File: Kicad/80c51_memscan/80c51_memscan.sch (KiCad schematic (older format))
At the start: 16 parts, among them J1 Conn_01x14_Male, J2 Conn_01x02_Male, SW1 SW_DPST_x2, U1 P80C51FA-4N,112, Y1 4-12Mhz

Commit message: Fixing typo 8051c -> 80c51.
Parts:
- U1: symbol 8051c_memscan-rescue:P80C51FA-4N,112-P80C51FA-4N_112 -> 80c51_memscan-rescue:P80C51FA-4N,112-P80C51FA-4N_112-8051c_memscan-rescue
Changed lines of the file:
@@
 EESchema Schematic File Version 4
-LIBS:8051c_memscan-cache
-EELAYER 29 0
+LIBS:80c51_memscan-cache
+EELAYER 26 0
 EELAYER END
 $Descr A4 11693 8268
 encoding utf-8
 Sheet 1 1
-Title "8051C Memory Scanner"
+Title "80C51 Memory Scanner"
 Date "2019-08-30"
 Rev "v1.0"
@@
 	3500 1900 3650 1900
 $Comp
-L 8051c_memscan-rescue:P80C51FA-4N,112-P80C51FA-4N_112 U1
+L 80c51_memscan-rescue:P80C51FA-4N,112-P80C51FA-4N_112-8051c_memscan-rescue U1
 U 1 1 5D70DC40
 P 5050 3550

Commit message: Folding in feedback. Adding led and additional pins to header.
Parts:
- added D1: LED, symbol Device:LED
- added R10: R, symbol Device:R
- J1: symbol Connector:Conn_01x14_Male -> Connector_Generic:Conn_02x16_Counter_Clockwise
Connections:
- net +5V: now also J1.17 (Pin_17), J1.18 (Pin_18), J1.19 (Pin_19), J1.20 (Pin_20), J1.21 (Pin_21), J1.22 (Pin_22), J1.23 (Pin_23), J1.24 (Pin_24), J1.25 (Pin_25), J1.26 (Pin_26), J1.27 (Pin_27), J1.28 (Pin_28), J1.29 (Pin_29), J1.30 (Pin_30), J1.31 (Pin_31), J1.32 (Pin_32), D1.2 (A), R10.2
- net 1 renamed A0
- net 10 renamed A9
- net 11 renamed A10
- net 12 renamed A11
- net 13 renamed A12
- net 14 renamed A13
- net 2 renamed A1
- net 3 renamed A2
- net 4 renamed A3
- net 5 renamed A4
- net 6 renamed A5
- net 7 renamed A6
- net 8 renamed A7
- net 9 renamed A8
- net xtal1 renamed XTAL1
- net xtal2 renamed XTAL2
- new net: D1.1 (K), R10.1
- no-connect marks 20 -> 22
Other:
- moved on the sheet: C1, C2, J2, R1, SW1A, U1, Y1

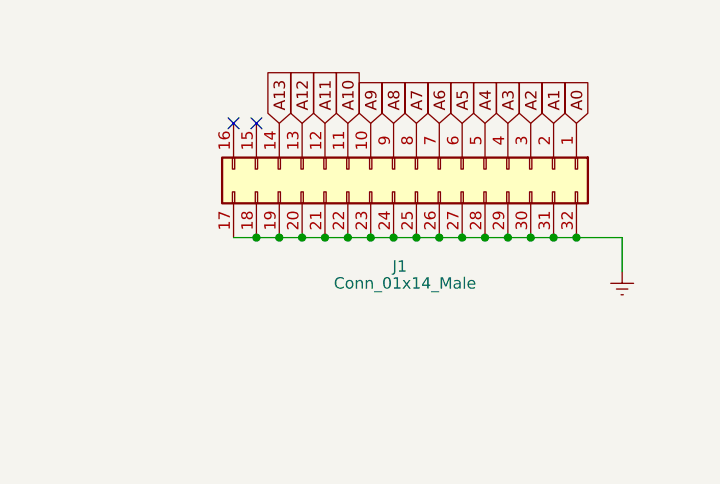
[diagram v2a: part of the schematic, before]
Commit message: Fix J1 text.
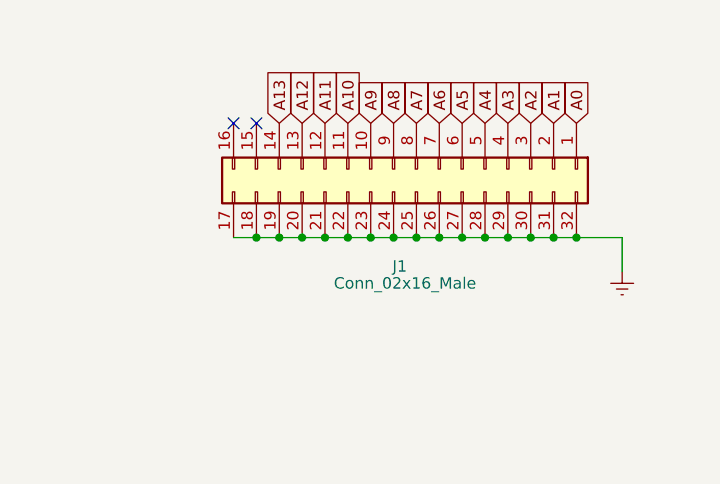
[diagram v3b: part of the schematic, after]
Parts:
- J1: value Conn_01x14_Male -> Conn_02x16_Male
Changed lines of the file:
@@
 P 8700 5000
 F 0 "J1" V 9126 4927 50  0000 C CNN
-F 1 "Conn_01x14_Male" V 9200 4950 50  0000 C CNN
+F 1 "Conn_02x16_Male" V 9200 4950 50  0000 C CNN
 F 2 "" H 8700 5000 50  0001 C CNN
 F 3 "~" H 8700 5000 50  0001 C CNN

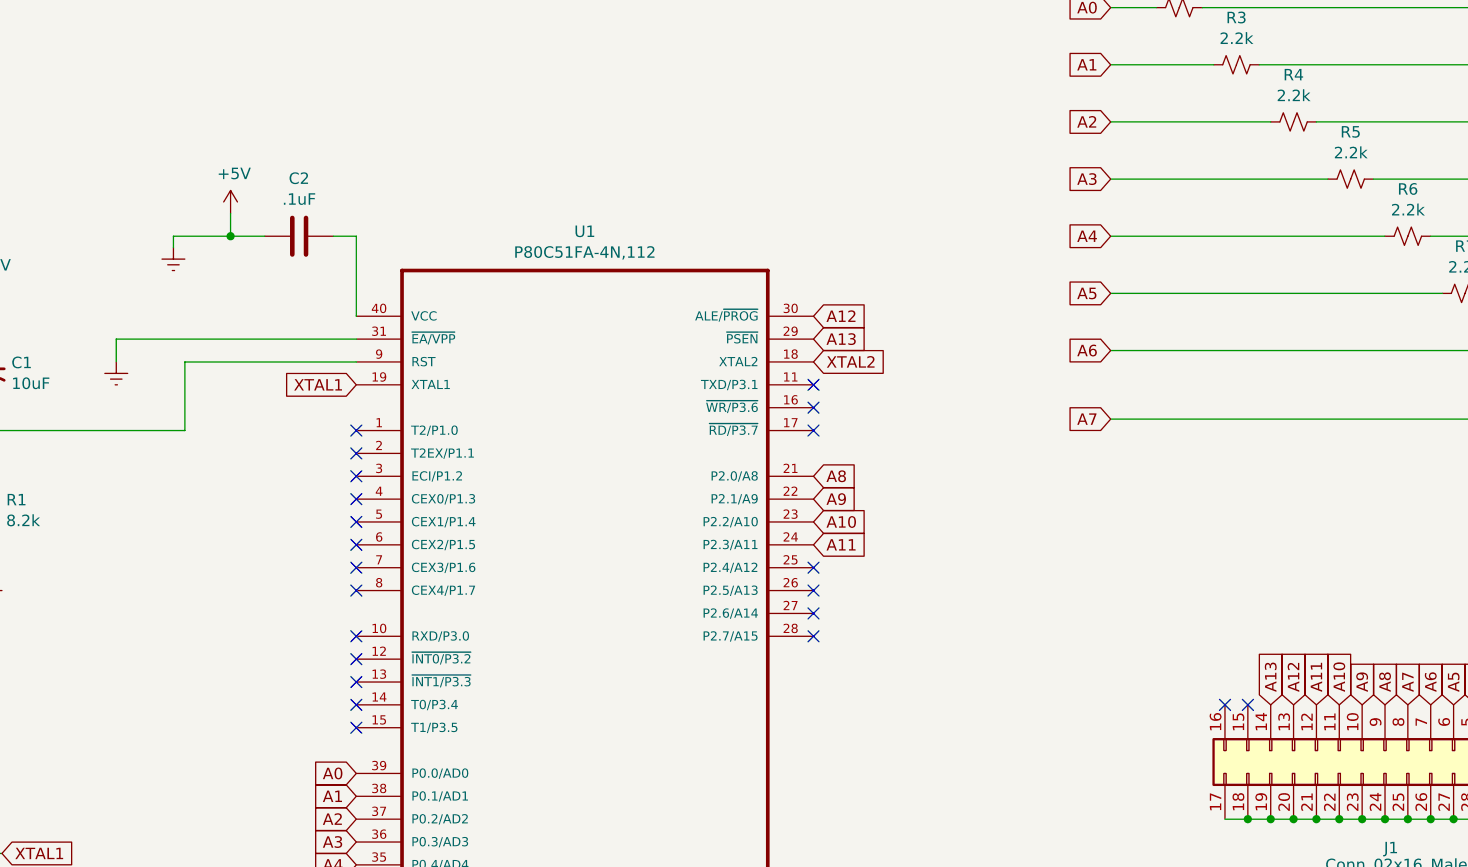
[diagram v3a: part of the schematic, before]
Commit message: Fixing bad cap wiring and some net names.
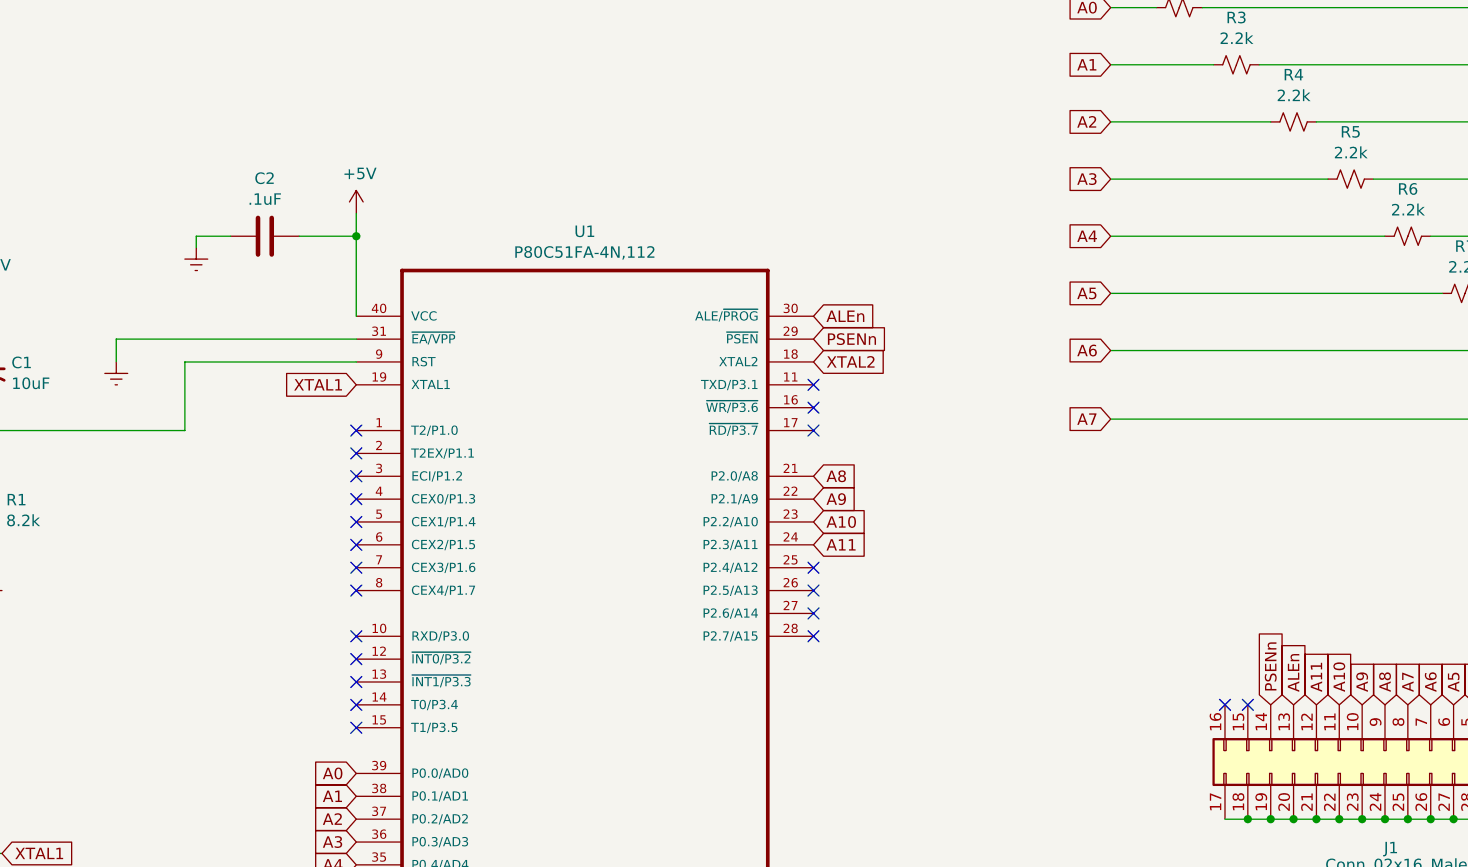
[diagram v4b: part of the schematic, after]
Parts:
- C1, C2, R1, R10, R2, R3, R4, R5, R6, R7, R8, R9: footprint (none) -> Capacitor_SMD:C_0603_1608Metric_Pad1.05x0.95mm_HandSolder
- D1: footprint (none) -> LED_SMD:LED_0603_1608Metric
- J1: footprint (none) -> Connector_PinHeader_2.54mm:PinHeader_2x16_P2.54mm_Vertical
- J2: footprint (none) -> Connector_PinHeader_2.54mm:PinHeader_1x02_P2.54mm_Vertical
- SW1: footprint (none) -> Button_Switch_SMD:SW_DIP_SPSTx02_Slide_6.7x6.64mm_W8.61mm_P2.54mm_LowProfile
- Y1: footprint (none) -> Crystal:Crystal_SMD_0603-2Pin_6.0x3.5mm_HandSoldering
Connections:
- net +5V: now also C2.2, U1.40 (VCC); no longer C2.1, J1.17 (Pin_17), J1.18 (Pin_18), J1.19 (Pin_19), J1.20 (Pin_20), J1.21 (Pin_21), J1.22 (Pin_22), J1.23 (Pin_23), J1.24 (Pin_24), J1.25 (Pin_25), J1.26 (Pin_26), J1.27 (Pin_27), J1.28 (Pin_28), J1.29 (Pin_29), J1.30 (Pin_30), J1.31 (Pin_31), J1.32 (Pin_32), J2.2 (Pin_2), R1.2, R10.2, R2.1, R3.1, R4.1, R5.1, R6.1, R7.1, R8.1, R9.1, U1.20 (VSS), U1.31 (~EA/VPP)
- net A12 renamed ALEn
- net A13 renamed PSENn
- new net Earth: C2.1, J1.17 (Pin_17), J1.18 (Pin_18), J1.19 (Pin_19), J1.20 (Pin_20), J1.21 (Pin_21), J1.22 (Pin_22), J1.23 (Pin_23), J1.24 (Pin_24), J1.25 (Pin_25), J1.26 (Pin_26), J1.27 (Pin_27), J1.28 (Pin_28), J1.29 (Pin_29), J1.30 (Pin_30), J1.31 (Pin_31), J1.32 (Pin_32), J2.2 (Pin_2), R1.2, R10.2, R2.1, R3.1, R4.1, R5.1, R6.1, R7.1, R8.1, R9.1, U1.20 (VSS), U1.31 (~EA/VPP)
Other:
- moved on the sheet: C2
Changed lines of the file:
@@
 F 0 "Y1" V 1904 5731 50  0000 L CNN
 F 1 "4-12Mhz" V 1995 5731 50  0000 L CNN
-F 2 "" H 1950 5600 50  0001 C CNN
+F 2 "Crystal:Crystal_SMD_0603-2Pin_6.0x3.5mm_HandSoldering" H 1950 5600 50  0001 C CNN
 F 3 "~" H 1950 5600 50  0001 C CNN
 	1    1950 5600
@@
 F 0 "C1" H 2591 3396 50  0000 L CNN
 F 1 "10uF" H 2591 3305 50  0000 L CNN
-F 2 "" H 2500 3350 50  0001 C CNN
+F 2 "Capacitor_SMD:C_0603_1608Metric_Pad1.05x0.95mm_HandSolder" H 2500 3350 50  0001 C CNN
 F 3 "~" H 2500 3350 50  0001 C CNN
 	1    2500 3350
@@
 F 0 "R1" H 2568 3996 50  0000 L CNN
 F 1 "8.2k" H 2568 3905 50  0000 L CNN
-F 2 "" H 2500 3950 50  0001 C CNN
+F 2 "Capacitor_SMD:C_0603_1608Metric_Pad1.05x0.95mm_HandSolder" H 2500 3950 50  0001 C CNN
 F 3 "~" H 2500 3950 50  0001 C CNN
 	1    2500 3950
@@
 L power:+5V #PWR05
 U 1 1 5D6AD917
-P 3550 2650
-F 0 "#PWR05" H 3550 2500 50  0001 C CNN
-F 1 "+5V" H 3565 2823 50  0000 C CNN
-F 2 "" H 3550 2650 50  0001 C CNN
-F 3 "" H 3550 2650 50  0001 C CNN
-	1    3550 2650
+P 4100 2650
+F 0 "#PWR05" H 4100 2500 50  0001 C CNN
+F 1 "+5V" H 4115 2823 50  0000 C CNN
+F 2 "" H 4100 2650 50  0001 C CNN
+F 3 "" H 4100 2650 50  0001 C CNN
+	1    4100 2650
 	1    0    0    -1
 $EndComp
@@
 F 0 "SW1" V 1746 3162 50  0000 R CNN
 F 1 "SW_DPST_x2" V 1655 3162 50  0000 R CNN
-F 2 "" H 1700 3250 50  0001 C CNN
+F 2 "Button_Switch_SMD:SW_DIP_SPSTx02_Slide_6.7x6.64mm_W8.61mm_P2.54mm_LowProfile" H 1700 3250 50  0001 C CNN
 F 3 "" H 1700 3250 50  0001 C CNN
 	1    1700 3250
@@
 L Device:C C2
 U 1 1 5D6AE417
-P 3850 2750
-F 0 "C2" V 4102 2750 50  0000 C CNN
-F 1 ".1uF" V 4011 2750 50  0000 C CNN
-F 2 "" H 3888 2600 50  0001 C CNN
-F 3 "~" H 3850 2750 50  0001 C CNN
-	1    3850 2750
+P 3700 2750
+F 0 "C2" V 3952 2750 50  0000 C CNN
+F 1 ".1uF" V 3861 2750 50  0000 C CNN
+F 2 "Capacitor_SMD:C_0603_1608Metric_Pad1.05x0.95mm_HandSolder" H 3738 2600 50  0001 C CNN
+F 3 "~" H 3700 2750 50  0001 C CNN
+	1    3700 2750
 	0    -1   -1   0
 $EndComp
@@
 L power:Earth #PWR07
 U 1 1 5D6AE7BB
-P 3300 2800
-F 0 "#PWR07" H 3300 2550 50  0001 C CNN
-F 1 "Earth" H 3300 2650 50  0001 C CNN
-F 2 "" H 3300 2800 50  0001 C CNN
-F 3 "~" H 3300 2800 50  0001 C CNN
-	1    3300 2800
+P 3400 2800
+F 0 "#PWR07" H 3400 2550 50  0001 C CNN
+F 1 "Earth" H 3400 2650 50  0001 C CNN
+F 2 "" H 3400 2800 50  0001 C CNN
+F 3 "~" H 3400 2800 50  0001 C CNN
+	1    3400 2800
 	1    0    0    -1
 $EndComp
@@
 F 0 "J1" V 9126 4927 50  0000 C CNN
 F 1 "Conn_02x16_Male" V 9200 4950 50  0000 C CNN
-F 2 "" H 8700 5000 50  0001 C CNN
+F 2 "Connector_PinHeader_2.54mm:PinHeader_2x16_P2.54mm_Vertical" H 8700 5000 50  0001 C CNN
 F 3 "~" H 8700 5000 50  0001 C CNN
 	1    8700 5000
@@
 $EndComp
 Wire Wire Line
-	3550 2750 3550 2650
-Connection ~ 3550 2750
-Wire Wire Line
-	3550 2750 3700 2750
+	4100 2750 4100 2650
 $Comp
 L 80c51_memscan-rescue:P80C51FA-4N,112-P80C51FA-4N_112-8051c_memscan-rescue U1
@@
 $EndComp
 Wire Wire Line
-	3300 2750 3300 2800
-Wire Wire Line
-	3300 2750 3550 2750
+	3400 2750 3400 2800
 Wire Wire Line
 	4100 3300 3350 3300
@@
 A11
 Text GLabel 8200 4800 1    50   Input ~ 0
-A12
+ALEn
 Text GLabel 8100 4800 1    50   Input ~ 0
-A13
-Wire Wire Line
-	4000 2750 4100 2750
+PSENn
 Wire Wire Line
 	4100 2750 4100 3100
@@
 A11
 Text GLabel 6100 3100 2    50   Input ~ 0
-A12
+ALEn
 Text GLabel 6100 3200 2    50   Input ~ 0
-A13
+PSENn
 NoConn ~ 4100 3600
 NoConn ~ 4100 3700
@@
 F 0 "R3" V 7745 2000 50  0000 C CNN
 F 1 "2.2k" V 7836 2000 50  0000 C CNN
-F 2 "" H 7950 2000 50  0001 C CNN
+F 2 "Capacitor_SMD:C_0603_1608Metric_Pad1.05x0.95mm_HandSolder" H 7950 2000 50  0001 C CNN
 F 3 "~" H 7950 2000 50  0001 C CNN
 	1    7950 2000
@@
 F 0 "R4" V 7995 2250 50  0000 C CNN
 F 1 "2.2k" V 8086 2250 50  0000 C CNN
-F 2 "" H 8200 2250 50  0001 C CNN
+F 2 "Capacitor_SMD:C_0603_1608Metric_Pad1.05x0.95mm_HandSolder" H 8200 2250 50  0001 C CNN
 F 3 "~" H 8200 2250 50  0001 C CNN
 	1    8200 2250
@@
 F 0 "R2" V 7495 1750 50  0000 C CNN
 F 1 "2.2k" V 7586 1750 50  0000 C CNN
-F 2 "" H 7700 1750 50  0001 C CNN
+F 2 "Capacitor_SMD:C_0603_1608Metric_Pad1.05x0.95mm_HandSolder" H 7700 1750 50  0001 C CNN
 F 3 "~" H 7700 1750 50  0001 C CNN
 	1    7700 1750
@@
 F 0 "R5" V 8245 2500 50  0000 C CNN
 F 1 "2.2k" V 8336 2500 50  0000 C CNN
-F 2 "" H 8450 2500 50  0001 C CNN
+F 2 "Capacitor_SMD:C_0603_1608Metric_Pad1.05x0.95mm_HandSolder" H 8450 2500 50  0001 C CNN
 F 3 "~" H 8450 2500 50  0001 C CNN
 	1    8450 2500
@@
 F 0 "R6" V 8495 2750 50  0000 C CNN
 F 1 "2.2k" V 8586 2750 50  0000 C CNN
-F 2 "" H 8700 2750 50  0001 C CNN
+F 2 "Capacitor_SMD:C_0603_1608Metric_Pad1.05x0.95mm_HandSolder" H 8700 2750 50  0001 C CNN
 F 3 "~" H 8700 2750 50  0001 C CNN
 	1    8700 2750
@@
 F 0 "R7" V 8745 3000 50  0000 C CNN
 F 1 "2.2k" V 8836 3000 50  0000 C CNN
-F 2 "" H 8950 3000 50  0001 C CNN
+F 2 "Capacitor_SMD:C_0603_1608Metric_Pad1.05x0.95mm_HandSolder" H 8950 3000 50  0001 C CNN
 F 3 "~" H 8950 3000 50  0001 C CNN
 	1    8950 3000
@@
 F 0 "R8" V 8995 3250 50  0000 C CNN
 F 1 "2.2k" V 9086 3250 50  0000 C CNN
-F 2 "" H 9200 3250 50  0001 C CNN
+F 2 "Capacitor_SMD:C_0603_1608Metric_Pad1.05x0.95mm_HandSolder" H 9200 3250 50  0001 C CNN
 F 3 "~" H 9200 3250 50  0001 C CNN
 	1    9200 3250
@@
 F 0 "R9" V 9245 3550 50  0000 C CNN
 F 1 "2.2k" V 9336 3550 50  0000 C CNN
-F 2 "" H 9450 3550 50  0001 C CNN
+F 2 "Capacitor_SMD:C_0603_1608Metric_Pad1.05x0.95mm_HandSolder" H 9450 3550 50  0001 C CNN
 F 3 "~" H 9450 3550 50  0001 C CNN
 	1    9450 3550
@@
 F 0 "J2" H 2008 1531 50  0000 C CNN
 F 1 "Conn_01x02_Male" H 2008 1440 50  0000 C CNN
-F 2 "" H 1900 1350 50  0001 C CNN
+F 2 "Connector_PinHeader_2.54mm:PinHeader_1x02_P2.54mm_Vertical" H 1900 1350 50  0001 C CNN
 F 3 "~" H 1900 1350 50  0001 C CNN
 	1    1900 1350
@@
 F 0 "D1" H 3192 1095 50  0000 C CNN
 F 1 "LED" H 3192 1186 50  0000 C CNN
-F 2 "" H 3200 1350 50  0001 C CNN
+F 2 "LED_SMD:LED_0603_1608Metric" H 3200 1350 50  0001 C CNN
 F 3 "~" H 3200 1350 50  0001 C CNN
 	1    3200 1350
@@
 F 0 "R10" V 4007 1350 50  0000 C CNN
 F 1 "R" V 3916 1350 50  0000 C CNN
-F 2 "" V 3730 1350 50  0001 C CNN
+F 2 "Capacitor_SMD:C_0603_1608Metric_Pad1.05x0.95mm_HandSolder" V 3730 1350 50  0001 C CNN
 F 3 "~" H 3800 1350 50  0001 C CNN
 	1    3800 1350
@@
 Wire Wire Line
 	9400 5300 9600 5300
+Wire Wire Line
+	3400 2750 3550 2750
+Connection ~ 4100 2750
+Wire Wire Line
+	3850 2750 4100 2750
 $EndSCHEMATC

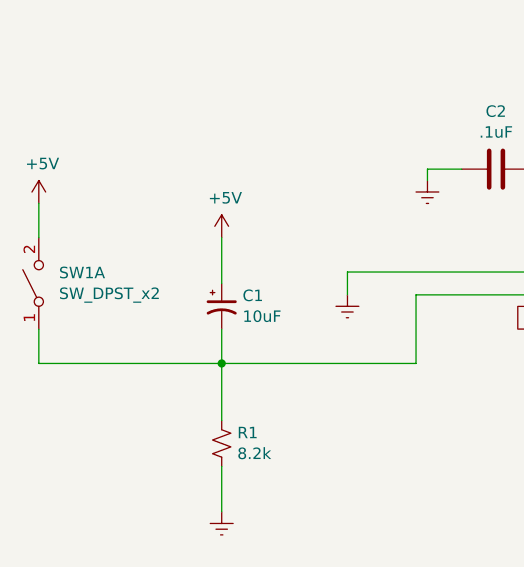
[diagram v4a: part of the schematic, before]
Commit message: Fixed switch symbol in schematic. And associated footprints for components.
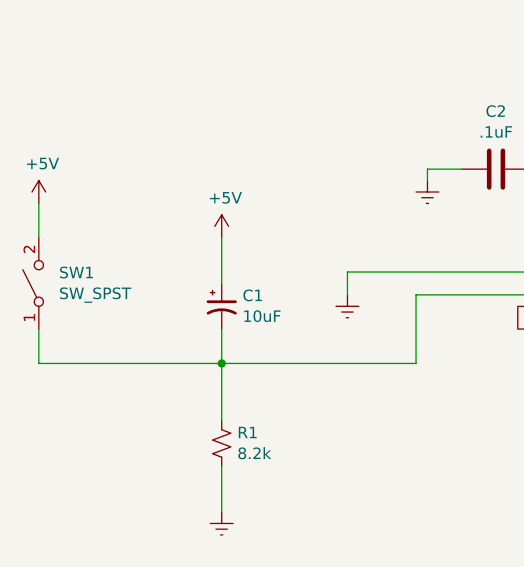
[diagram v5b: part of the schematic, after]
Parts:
- removed SW1: SW_DPST_x2, Button_Switch_SMD:SW_DIP_SPSTx02_Slide_6.7x6.64mm_W8.61mm_P2.54mm_LowProfile, symbol Switch:SW_DPST_x2
- added SW1: SW_SPST, symbol Switch:SW_SPST
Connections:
- net +5V: now also SW1.2 (B)
- net at C1.2, R1.1, U1.9 (RST): now also SW1.1 (A)
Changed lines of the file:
@@
-$EndComp
-$Comp
-L Switch:SW_DPST_x2 SW1
-U 1 1 5D6AE32B
-P 1700 3250
-F 0 "SW1" V 1746 3162 50  0000 R CNN
-F 1 "SW_DPST_x2" V 1655 3162 50  0000 R CNN
-F 2 "Button_Switch_SMD:SW_DIP_SPSTx02_Slide_6.7x6.64mm_W8.61mm_P2.54mm_LowProfile" H 1700 3250 50  0001 C CNN
-F 3 "" H 1700 3250 50  0001 C CNN
-	1    1700 3250
-	0    -1   -1   0
 $EndComp
 $Comp
@@
 Wire Wire Line
 	3850 2750 4100 2750
+$Comp
+L Switch:SW_SPST SW1
+U 1 1 5D7405E0
+P 1700 3250
+F 0 "SW1" V 1746 3162 50  0000 R CNN
+F 1 "SW_SPST" V 1655 3162 50  0000 R CNN
+F 2 "" H 1700 3250 50  0001 C CNN
+F 3 "" H 1700 3250 50  0001 C CNN
+	1    1700 3250
+	0    -1   -1   0
+$EndComp
 $EndSCHEMATC

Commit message: Associated footprints. Starting pcb layout.
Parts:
- SW1: footprint (none) -> Button_Switch_THT:SW_DIP_SPSTx01_Slide_9.78x4.72mm_W7.62mm_P2.54mm
- U1: footprint DIP254P1524X470-40 -> P80C51FA-4N_112:DIP254P1524X470-40
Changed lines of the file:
@@
 F 0 "U1" H 5100 6070 50  0000 C CNN
 F 1 "P80C51FA-4N,112" H 5100 5979 50  0000 C CNN
-F 2 "DIP254P1524X470-40" H 5100 4400 50  0001 L BNN
+F 2 "P80C51FA-4N_112:DIP254P1524X470-40" H 5100 4400 50  0001 L BNN
 F 3 "None" H 5100 4400 50  0001 L BNN
 F 4 "NXP USA" H 5100 4400 50  0001 L BNN "Field4"
@@
 F 0 "SW1" V 1746 3162 50  0000 R CNN
 F 1 "SW_SPST" V 1655 3162 50  0000 R CNN
-F 2 "" H 1700 3250 50  0001 C CNN
+F 2 "Button_Switch_THT:SW_DIP_SPSTx01_Slide_9.78x4.72mm_W7.62mm_P2.54mm" H 1700 3250 50  0001 C CNN
 F 3 "" H 1700 3250 50  0001 C CNN
 	1    1700 3250
